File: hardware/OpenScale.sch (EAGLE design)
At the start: 59 parts, among them Q1 200mA/50V, Q2 200mA/50V, U1 HX711, U3 TMP102, U4 ATMEGA328P_TQFP, U5 MIC52055-5V, U6 FT231X, Y2 16MHZ

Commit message: Remove v-reg add PNP for internal v-reg.
Added 4.7k pull up for One Wire external temp.
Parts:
- removed C14, C15: 10uF, SparkFun-Capacitors:10UF-16V-10%(TANT)
- removed C18: 470pF, SparkFun-Capacitors:470PF-50V-5%(0603)SMD
- removed R10: 100, SparkFun-Resistors:100OHM-1/10W-1%(0603)
- removed U5: MIC52055-5V, SparkFun-PowerIC:MIC52055V
- added C11: 0.1uF, SparkFun-Capacitors:0.1UF-25V(+80/-20%)(0603)
- added C12, C13: 1.0uF, SparkFun-Capacitors:1.0UF-16V-10%(0603)
- added LOGO3: SFE_LOGO_FLAME.1EXP, SparkFun-Aesthetics:SFE_LOGO_FLAME.1EXP
- added Q3: MMBT4403, SparkFun-DiscreteSemi:TRANSISTOR_PNPMMBT4403
- added R14: 4.7K, SparkFun-Resistors:4.7KOHM-1/10W-1%(0603)
- added R16: 20K, SparkFun-Resistors:20KOHM1/10W1%(0603)
- added R17: 8.2K, SparkFun-Resistors:8.2KOHM-1/10W-5%(0603)
- C16, C3, C8: device SparkFun-Capacitors:0.1UF-25V-5%(0603) -> SparkFun-Capacitors:0.1UF-25V(+80/-20%)(0603)
- JP2: value M02PTH -> (none)
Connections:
- removed net AMP_EN: U4.PC2(ADC2), U5.EN
- removed net N$15: C18.1, U5.BP
- new net N$17: Q3.B, U1.BASE
- new net N$18: R16.1, R17.2, U1.VFB
- new net N$21: C11.2, U1.VBG
- net 5V: now also C13.1, Q3.E, R14.2; no longer C14.+, U5.IN
- net AVDD: now also C12.2, Q3.C, R16.2; no longer C15.+, R10.2, U5.OUT
- net GND: now also C11.1, C12.1, C13.2, R17.1; no longer C14.-, C15.-, C18.2, R10.1, U1.VFB, U5.GND
- net TEMP_DAT: now also R14.1
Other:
- note added: "AVDD = VBG(R1+R2)/R1"
- note added: "VBG = 1.25V"
- note removed: "Add GND label to RJ45"
- note removed: "Convert v-reg to adjustable and output 4.7V"
- note removed: "Correct silk to DTR on FTDI"
- note removed: "Fix flame over ISP"
- note removed: "Low noise regulator"
- note removed: "Not sure about this v-reg. 5V from USB may not be enough to clean up AVDD."
- note removed: "Outline the flame in tDocu in library"
- note removed: "add 4.7k to ds18b20"
- note removed: "change ds18s20 to ds18x20"
- moved on the sheet: C16, C3, C8, JP1, JP2, JP3, JP6, Q1, Q2, R3, R4, R7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

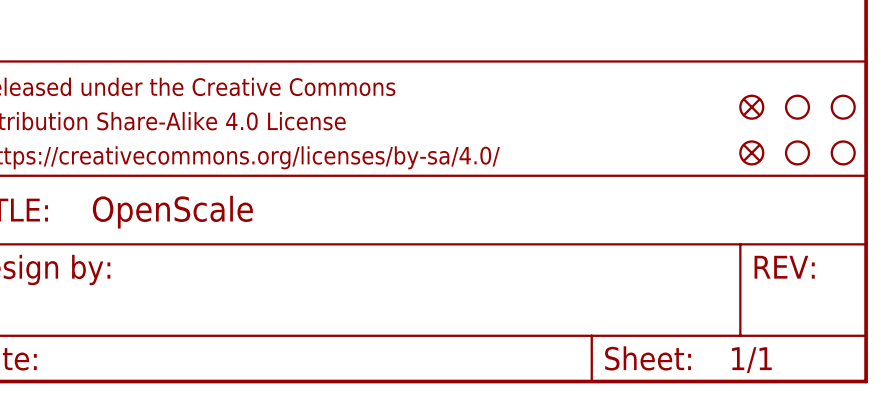
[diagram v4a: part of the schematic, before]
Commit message: Fixed issue 4 - DRC errors and schematic markings.
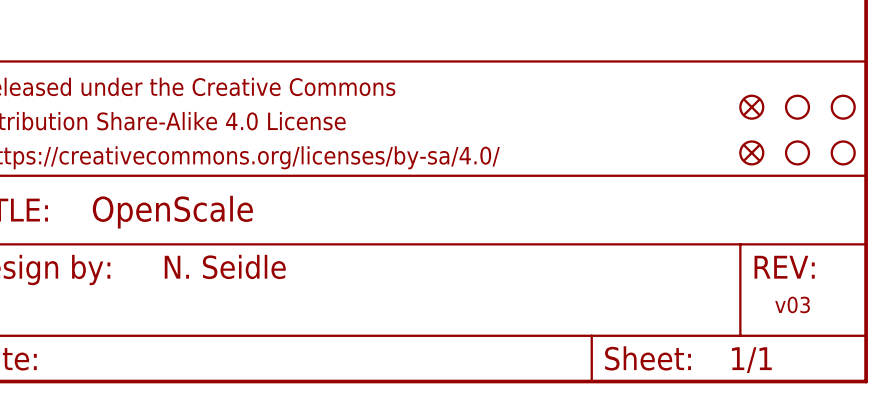
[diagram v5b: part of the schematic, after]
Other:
- note added: "N. Seidle"
- note added: "v03"
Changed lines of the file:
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@@
 <text x="309.88" y="162.56" size="1.778" layer="96">VBG = 1.25V</text>
 <text x="259.08" y="165.1" size="1.778" layer="96">AVDD = VBG(R1+R2)/R1</text>
+<text x="421.64" y="7.62" size="1.778" layer="94">v03</text>
+<text x="353.568" y="11.43" size="2.54" layer="94">N. Seidle</text>
 </plain>
 <instances>

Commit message: Crazy re-design to use screw terminals.
Rather than RJ45 I have moved to screw terminals. This should make it
easy on end customers who don't have a solder iron to get up and running
immediately.
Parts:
- added JP4: Screw, SparkFun-Connectors:M03SCREW_LOCK
- added JP8: (no value), SparkFun-Connectors:M023.5MM_LOCK
- JP6: value RJ45 -> (none); device SparkFun-Connectors:RJ45-8PTH -> SparkFun-Connectors:M03SCREW_LOCK
- LOGO3: value SFE_LOGO_FLAME.1EXP -> SFE_LOGO_FLAME.1_STOP; device SparkFun-Aesthetics:SFE_LOGO_FLAME.1EXP -> SparkFun-Aesthetics:SFE_LOGO_FLAME.1_STOP
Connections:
- net 5V: now also JP4.1; no longer JP6.3
- net A+: now also JP8.1; no longer JP6.5
- net A-: now also JP6.3; no longer JP6.4
- net AVDD: now also JP6.1; no longer JP6.8
- net GND: now also JP4.3, JP6.2, JP8.2; no longer JP6.1, JP6.6, JP6.7
- net TEMP_DAT: now also JP4.2; no longer JP6.2
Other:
- note added: "Screw Terminals"
- note removed: "Optional Pluggable Connection"
- moved on the sheet: C1, C10, C11, C12, C13, C16, C2, C3, C4, C5, C6, C7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

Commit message: New version with screw terminals. Ready for review.
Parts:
- JP1: device SparkFun-Connectors:M03PTH -> SparkFun-Connectors:M031X03_NO_SILK
- JP3: device SparkFun-Connectors:M05PTH -> SparkFun-Connectors:M05NO_SILK
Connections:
- net GND: now also JP9.5
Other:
- note added: "Power the board with 4.5-5.5V"
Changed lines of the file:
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@@
 <part name="U$8" library="SparkFun" deviceset="5V" device=""/>
 <part name="U$9" library="SparkFun" deviceset="5V" device=""/>
-<part name="JP1" library="SparkFun-Connectors" deviceset="M03" device="PTH"/>
+<part name="JP1" library="SparkFun-Connectors" deviceset="M03" device="1X03_NO_SILK"/>
 <part name="U$16" library="SparkFun" deviceset="5V" device=""/>
 <part name="GND1" library="SparkFun-Aesthetics" deviceset="GND" device=""/>
@@
 <part name="Y2" library="SparkFun-FreqCtrl" deviceset="RESONATOR" device="16MHZ" value="16MHZ"/>
 <part name="SJ2" library="SparkFun-Passives" deviceset="JUMPER-PAD-2-NC_BY_TRACE" device="" value=""/>
-<part name="JP3" library="SparkFun-Connectors" deviceset="M05" device="PTH"/>
 <part name="JP2" library="SparkFun-Connectors" deviceset="M02" device="PTH"/>
 <part name="C16" library="SparkFun-Capacitors" deviceset="0.1UF-25V(+80/-20%)(0603)" device="" value="0.1uF"/>
@@
 <part name="JP6" library="SparkFun-Connectors" deviceset="M03" device="SCREW_LOCK"/>
 <part name="JP8" library="SparkFun-Connectors" deviceset="M02" device="3.5MM_LOCK"/>
+<part name="JP3" library="SparkFun-Connectors" deviceset="M05" device="NO_SILK"/>
 </parts>
 <sheets>
@@
 <wire x1="17.78" y1="261.62" x2="17.78" y2="190.5" width="0.4064" layer="97" style="shortdash"/>
 <wire x1="182.88" y1="261.62" x2="182.88" y2="190.5" width="0.4064" layer="97" style="shortdash"/>
-<wire x1="30.48" y1="38.1" x2="30.48" y2="167.64" width="0.4064" layer="97" style="shortdash"/>
-<wire x1="170.18" y1="167.64" x2="30.48" y2="167.64" width="0.4064" layer="97" style="shortdash"/>
+<wire x1="30.48" y1="38.1" x2="30.48" y2="180.34" width="0.4064" layer="97" style="shortdash"/>
+<wire x1="170.18" y1="180.34" x2="30.48" y2="180.34" width="0.4064" layer="97" style="shortdash"/>
 <wire x1="170.18" y1="38.1" x2="30.48" y2="38.1" width="0.4064" layer="97" style="shortdash"/>
-<wire x1="170.18" y1="38.1" x2="170.18" y2="167.64" width="0.4064" layer="97" style="shortdash"/>
+<wire x1="170.18" y1="38.1" x2="170.18" y2="180.34" width="0.4064" layer="97" style="shortdash"/>
 <text x="33.02" y="162.56" size="2.54" layer="97">Microcontroller</text>
 <text x="20.32" y="256.54" size="2.54" layer="97">USB-Serial</text>
@@
 <text x="421.64" y="7.62" size="1.778" layer="94">v03</text>
 <text x="353.568" y="11.43" size="2.54" layer="94">N. Seidle</text>
+<text x="124.46" y="168.91" size="1.778" layer="97">Power the board with 4.5-5.5V</text>
 </plain>
 <instances>
@@
 </instance>
 <instance part="SJ2" gate="G$1" x="355.6" y="134.62" rot="R90"/>
-<instance part="JP3" gate="G$1" x="223.52" y="134.62"/>
 <instance part="JP2" gate="G$1" x="223.52" y="78.74"/>
 <instance part="C16" gate="G$1" x="281.94" y="129.54" rot="MR0"/>
@@
 <instance part="JP6" gate="G$1" x="223.52" y="111.76" rot="MR180"/>
 <instance part="JP8" gate="G$1" x="223.52" y="99.06" rot="MR180"/>
+<instance part="JP3" gate="G$1" x="223.52" y="134.62"/>
 </instances>
 <busses>
@@
 <wire x1="231.14" y1="129.54" x2="233.68" y2="129.54" width="0.1524" layer="91"/>
 <junction x="233.68" y="129.54"/>
-<pinref part="JP3" gate="G$1" pin="1"/>
-<pinref part="JP3" gate="G$1" pin="4"/>
 <wire x1="231.14" y1="96.52" x2="233.68" y2="96.52" width="0.1524" layer="91"/>
 <junction x="233.68" y="96.52"/>
 <pinref part="JP6" gate="G$1" pin="2"/>
 <pinref part="JP8" gate="G$1" pin="2"/>
+<pinref part="JP3" gate="G$1" pin="1"/>
+<pinref part="JP3" gate="G$1" pin="4"/>
 </segment>
 <segment>
@@
 <pinref part="GND13" gate="1" pin="GND"/>
 <pinref part="JP9" gate="G$1" pin="6"/>
+<pinref part="JP9" gate="G$1" pin="5"/>
+<wire x1="149.86" y1="147.32" x2="147.32" y2="147.32" width="0.1524" layer="91"/>
+<wire x1="147.32" y1="147.32" x2="147.32" y2="144.78" width="0.1524" layer="91"/>
+<junction x="147.32" y="144.78"/>
 </segment>
 <segment>
@@
 <wire x1="243.84" y1="114.3" x2="243.84" y2="139.7" width="0.1524" layer="91"/>
 <junction x="243.84" y="139.7"/>
-<pinref part="JP3" gate="G$1" pin="5"/>
 <wire x1="256.54" y1="139.7" x2="256.54" y2="142.24" width="0.1524" layer="91"/>
 <junction x="256.54" y="139.7"/>
@@
 <junction x="281.94" y="139.7"/>
 <pinref part="JP6" gate="G$1" pin="1"/>
+<pinref part="JP3" gate="G$1" pin="5"/>
 </segment>
 </net>
@@
 <wire x1="246.38" y1="109.22" x2="246.38" y2="134.62" width="0.1524" layer="91"/>
 <junction x="246.38" y="134.62"/>
-<pinref part="JP3" gate="G$1" pin="3"/>
 <pinref part="JP6" gate="G$1" pin="3"/>
 <wire x1="246.38" y1="109.22" x2="231.14" y2="109.22" width="0.1524" layer="91"/>
 <label x="236.22" y="109.22" size="1.778" layer="95"/>
+<pinref part="JP3" gate="G$1" pin="3"/>
 </segment>
 </net>
@@
 <junction x="248.92" y="132.08"/>
 <label x="236.22" y="99.06" size="1.778" layer="95"/>
-<pinref part="JP3" gate="G$1" pin="2"/>
 <wire x1="248.92" y1="99.06" x2="231.14" y2="99.06" width="0.1524" layer="91"/>
 <pinref part="JP8" gate="G$1" pin="1"/>
-</segment>
-</net>
+<pinref part="JP3" gate="G$1" pin="2"/>
+</segment>
+</net>

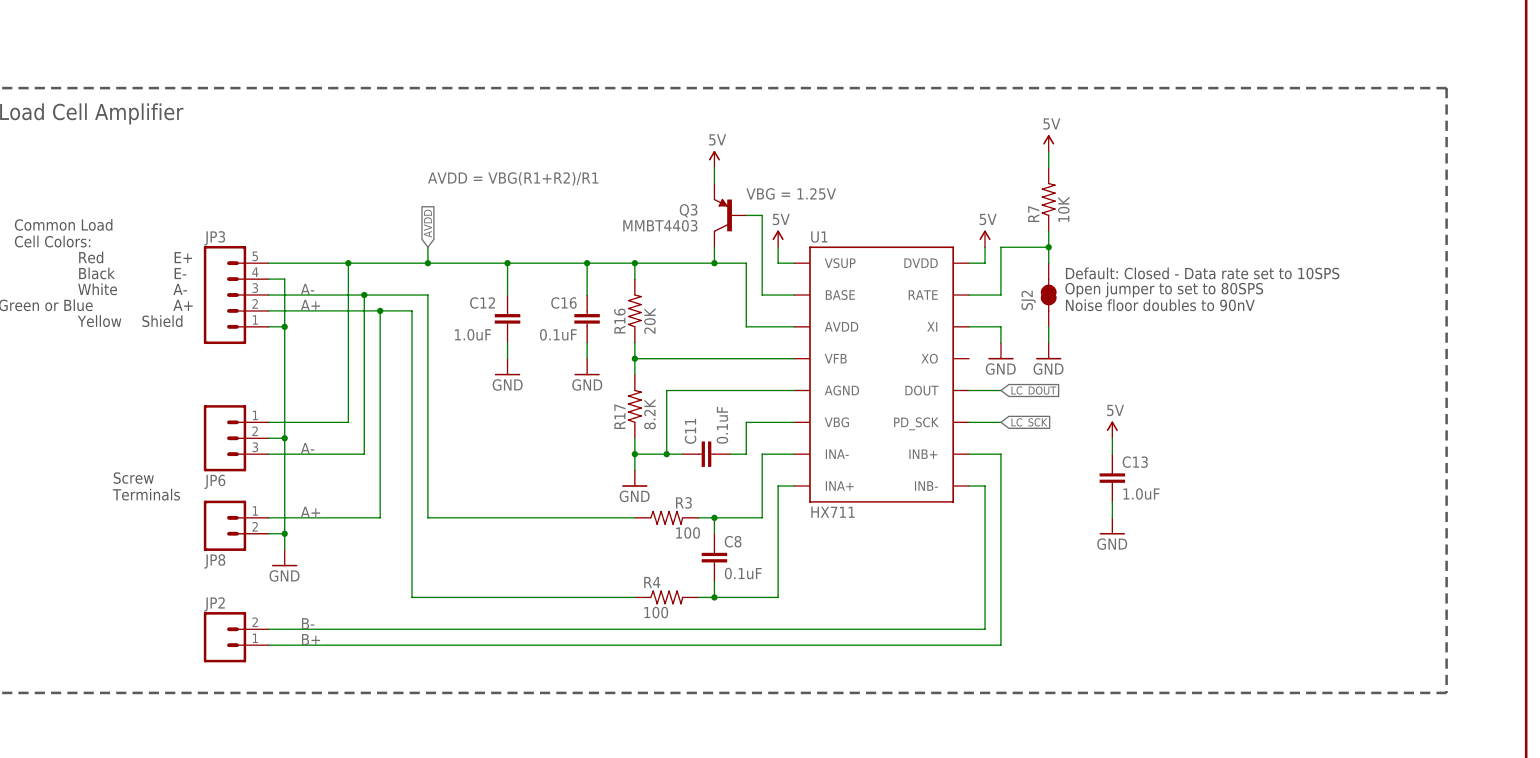
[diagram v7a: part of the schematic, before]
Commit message: Fix screw terminal spacing. Small firmware changes.
Footprint error on the screw terminals that prevented them from being
linked together (spaced too far apart). Should be fixed now but needs
double checking.
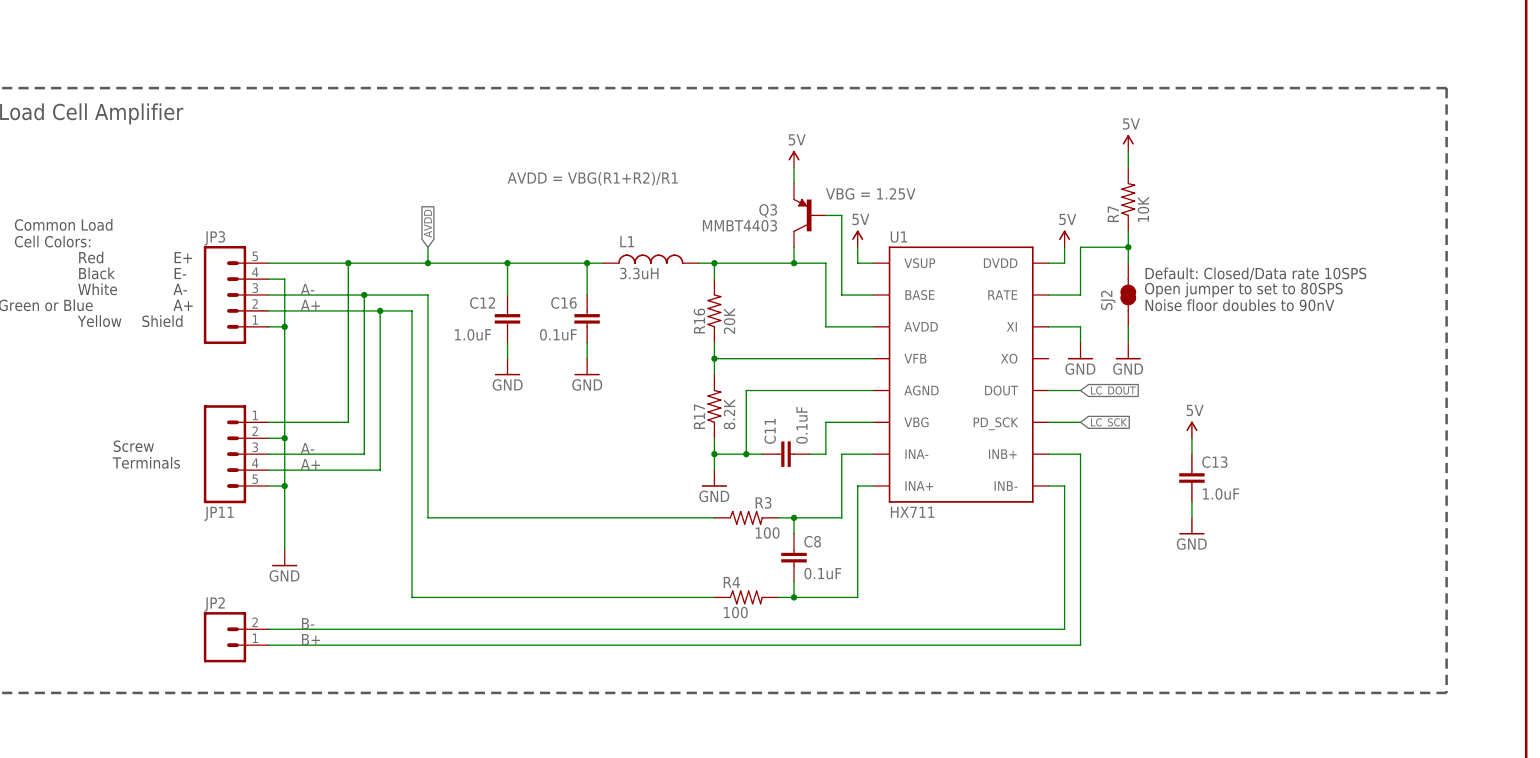
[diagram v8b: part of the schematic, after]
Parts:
- removed JP6: (no value), SparkFun-Connectors:M03SCREW_LOCK
- removed JP8: (no value), SparkFun-Connectors:M023.5MM_LOCK
- added JP11: (no value), SparkFun-Connectors:M05SCREW
- added L1: 3.3uH, SparkFun-Passives:INDUCTOR0805
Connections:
- new net N$15: L1.2, Q3.C, R16.2, U1.AVDD
- net A+: now also JP11.4; no longer JP8.1
- net A-: now also JP11.3; no longer JP6.3
- net AVDD: now also JP11.1, L1.1; no longer JP6.1, Q3.C, R16.2, U1.AVDD
- net GND: now also JP11.2, JP11.5; no longer JP6.2, JP8.2
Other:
- note added: "Default: Closed/Data rate 10SPS"
- note removed: "Default: Closed - Data rate set to 10SPS"
- moved on the sheet: C11, C13, C8, Q3, R16, R17, R3, R4, R7, SJ2, U1
